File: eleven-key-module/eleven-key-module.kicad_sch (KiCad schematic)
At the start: 90 parts, among them J1 +24V, J2 FPGA PWM Outputs, Q1 2N7000, Q10 IRLB8721PBF, Q11 2N7000, Q12 IRLB8721PBF, Q13 2N7000, Q14 IRLB8721PBF, Q15 2N7000, Q16 IRLB8721PBF, Q17 2N7000, Q18 IRLB8721PBF, Q19 2N7000, Q2 IRLB8721PBF, Q20 IRLB8721PBF, Q21 2N7000, Q22 IRLB8721PBF, Q3 2N7000, Q4 IRLB8721PBF, Q5 2N7000, Q6 IRLB8721PBF, Q7 2N7000, Q8 IRLB8721PBF, Q9 2N7000

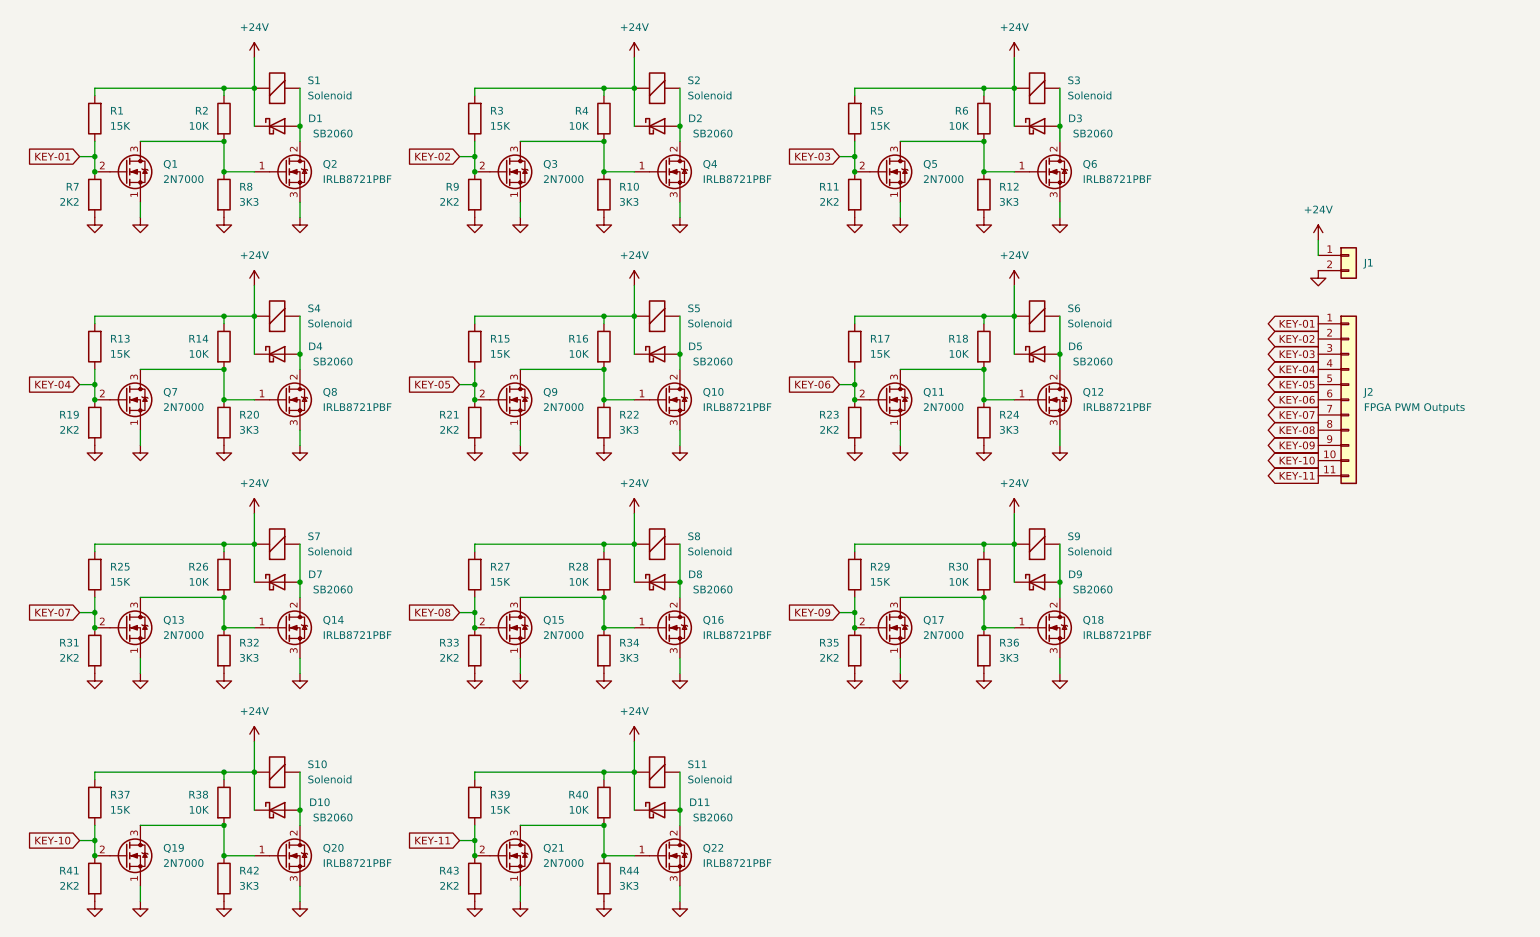
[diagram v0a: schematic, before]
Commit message: Switch schematic to Atmega328P
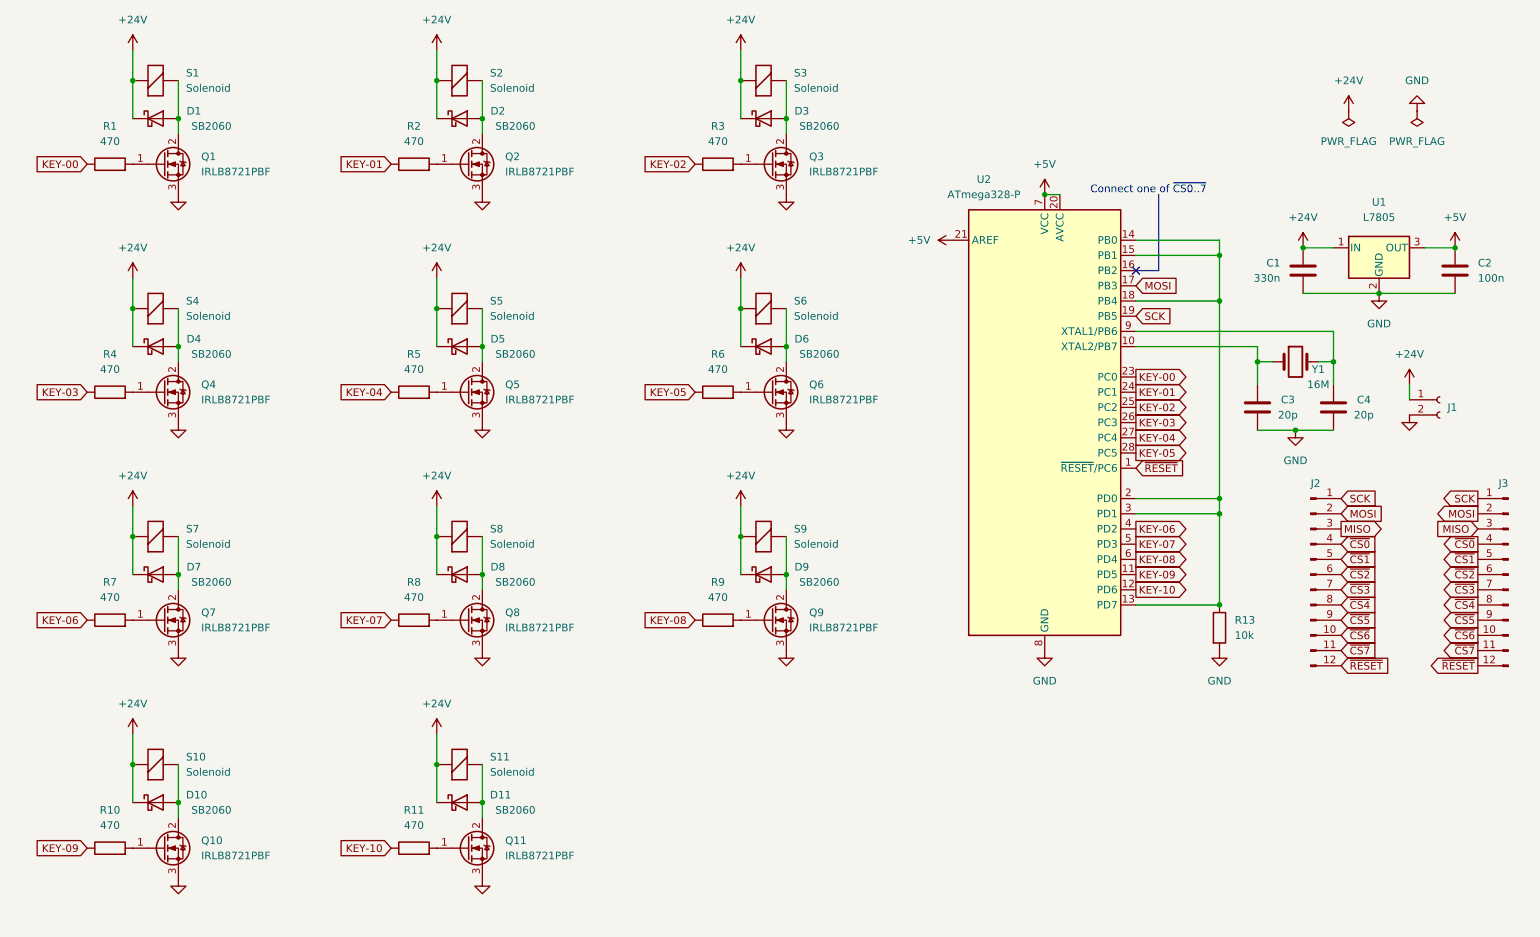
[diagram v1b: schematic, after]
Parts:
- removed J1: +24V, TerminalBlock_TE-Connectivity:TerminalBlock_TE_282834-2_1x02_P2.54mm_Horizontal, symbol Connector_Generic:Conn_01x02
- removed J2: FPGA PWM Outputs, Connector_JST:JST_XH_S11B-XH-A_1x11_P2.50mm_Horizontal, symbol Connector_Generic:Conn_01x11
- removed Q1, Q11, Q13, Q15, Q17, Q19, Q21, Q3, Q5, Q7, Q9: 2N7000, Package_TO_SOT_THT:TO-92_Inline, symbol Transistor_FET:2N7000
- removed Q12, Q14, Q16, Q18, Q20, Q22: IRLB8721PBF, Package_TO_SOT_THT:TO-220-3_Vertical, symbol Transistor_FET:IRLB8721PBF
- removed R12, R20, R22, R24, R32, R34, R36, R42, R44: 3K3, Resistor_THT:R_Axial_DIN0204_L3.6mm_D1.6mm_P2.54mm_Vertical, symbol Device:R
- removed R14, R16, R18, R26, R28, R30, R38, R40: 10K, Resistor_THT:R_Axial_DIN0204_L3.6mm_D1.6mm_P2.54mm_Vertical, symbol Device:R
- removed R15, R17, R25, R27, R29, R37, R39: 15K, Resistor_THT:R_Axial_DIN0204_L3.6mm_D1.6mm_P2.54mm_Vertical, symbol Device:R
- removed R19, R21, R23, R31, R33, R35, R41, R43: 2K2, Resistor_THT:R_Axial_DIN0204_L3.6mm_D1.6mm_P2.54mm_Vertical, symbol Device:R
- added C1: 330n, Capacitor_THT:C_Rect_L4.0mm_W2.5mm_P2.50mm, symbol Device:C
- added C2: 100n, Capacitor_THT:C_Rect_L4.0mm_W2.5mm_P2.50mm, symbol Device:C
- added C3, C4: 20p, Capacitor_THT:C_Disc_D3.4mm_W2.1mm_P2.50mm, symbol Device:C
- added J1: Conn_01x02_Female, symbol Connector:Conn_01x02_Female
- added J2, J3: Conn_01x12_Male, symbol Connector:Conn_01x12_Male
- added Q1, Q11, Q3, Q5, Q7, Q9: IRLB8721PBF, Package_TO_SOT_THT:TO-220-3_Vertical, symbol Transistor_FET:IRLB8721PBF
- added U1: L7805, Package_TO_SOT_THT:TO-220-3_Vertical, symbol Regulator_Linear:L7805
- added U2: ATmega328-P, Package_DIP:DIP-28_W7.62mm, symbol MCU_Microchip_ATmega:ATmega328-P
- added Y1: 16M, symbol Device:Crystal
- R1, R3, R5: value 15K -> 470; footprint Resistor_THT:R_Axial_DIN0204_L3.6mm_D1.6mm_P2.54mm_Vertical -> (none)
- R10, R8: value 3K3 -> 470; footprint Resistor_THT:R_Axial_DIN0204_L3.6mm_D1.6mm_P2.54mm_Vertical -> (none)
- R11, R7, R9: value 2K2 -> 470; footprint Resistor_THT:R_Axial_DIN0204_L3.6mm_D1.6mm_P2.54mm_Vertical -> (none)
- R13: value 15K -> 10k; footprint Resistor_THT:R_Axial_DIN0204_L3.6mm_D1.6mm_P2.54mm_Vertical -> (none)
- R2, R4, R6: value 10K -> 470; footprint Resistor_THT:R_Axial_DIN0204_L3.6mm_D1.6mm_P2.54mm_Vertical -> (none)
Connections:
- net +24V: now also C1.1, J1.1 (Pin_1), U1.1 (IN); no longer R1.2, R13.2, R2.1, R3.2, R4.1, R5.2, R6.1
- net GND: now also R13.2, C1.2, C2.2, C3.1, C4.1, J1.2 (Pin_2), Q1.3 (S), Q11.3 (S), Q3.3 (S), Q5.3 (S), Q7.3 (S), Q9.3 (S), U1.2 (GND), U2.22 (GND), U2.8 (GND); no longer R10.2, R11.2, R7.2, R8.2, R9.2
- net KEY-01: now also R2.1, U2.24 (PC1); no longer R1.1, R7.1
- net KEY-02: now also U2.25 (PC2); no longer R9.1
- net KEY-03: now also R4.1, U2.26 (PC3); no longer R11.1, R5.1
- net KEY-04: now also R5.1, U2.27 (PC4); no longer R13.1
- net KEY-05: now also R6.1, U2.28 (PC5)
- net KEY-06: now also R7.1, U2.4 (PD2)
- net KEY-07: now also R8.1, U2.5 (PD3)
- net KEY-08: now also R9.1, U2.6 (PD4)
- net KEY-09: now also R10.1, U2.11 (PD5)
- net KEY-10: now also R11.1, U2.12 (PD6)
- net at Q2.1 (G), R2.2: no longer R8.1
- net at D2.2 (A), S2.2 (+): now also Q2.2 (D); no longer Q4.2 (D)
- net at D1.2 (A), S1.2 (+): now also Q1.2 (D); no longer Q2.2 (D)
- net at Q4.1 (G), R4.2: no longer R10.1
- net at D8.2 (A), S8.2 (+): now also Q8.2 (D)
- net at D9.2 (A), S9.2 (+): now also Q9.2 (D)
- net at D10.2 (A), S10.2 (+): now also Q10.2 (D)
- net at D7.2 (A), S7.2 (+): now also Q7.2 (D)
- net at Q10.1 (G): now also R10.2
- net at D5.2 (A), S5.2 (+): now also Q5.2 (D); no longer Q10.2 (D)
- net at D6.2 (A), S6.2 (+): now also Q6.2 (D)
- net at D3.2 (A), S3.2 (+): now also Q3.2 (D); no longer Q6.2 (D)
- net at D11.2 (A), S11.2 (+): now also Q11.2 (D)
- net at D4.2 (A), S4.2 (+): now also Q4.2 (D); no longer Q8.2 (D)
- net at Q8.1 (G): now also R8.2
- new net: Q5.1 (G), R5.2
- new net: Q9.1 (G), R9.2
- new net: C3.2, U2.10 (XTAL2/PB7), Y1.1
- new net: R13.1, U2.13 (PD7), U2.14 (PB0), U2.15 (PB1), U2.18 (PB4), U2.2 (PD0), U2.3 (PD1)
- new net: C4.2, U2.9 (XTAL1/PB6), Y1.2
- new net: Q11.1 (G), R11.2
- new net: Q7.1 (G), R7.2
- new net: Q1.1 (G), R1.2
- new net: Q3.1 (G), R3.2
- new net +5V: C2.1, U1.3 (OUT), U2.20 (AVCC), U2.21 (AREF), U2.7 (VCC)
- new net KEY-00: R1.1, U2.23 (PC0)
- new net MISO: J2.3 (Pin_3), J3.3 (Pin_3)
- new net MOSI: J2.2 (Pin_2), J3.2 (Pin_2), U2.17 (PB3)
- new net SCK: J2.1 (Pin_1), J3.1 (Pin_1), U2.19 (PB5)
- new net ~{CS0}: J2.4 (Pin_4), J3.4 (Pin_4)
- new net ~{CS1}: J2.5 (Pin_5), J3.5 (Pin_5)
- new net ~{CS2}: J2.6 (Pin_6), J3.6 (Pin_6)
- new net ~{CS3}: J2.7 (Pin_7), J3.7 (Pin_7)
- new net ~{CS4}: J2.8 (Pin_8), J3.8 (Pin_8)
- new net ~{CS5}: J2.9 (Pin_9), J3.9 (Pin_9)
- new net ~{CS6}: J2.10 (Pin_10), J3.10 (Pin_10)
- new net ~{CS7}: J2.11 (Pin_11), J3.11 (Pin_11)
- new net ~{RESET}: J2.12 (Pin_12), J3.12 (Pin_12), U2.1 (~{RESET}/PC6)
- no-connect marks 0 -> 1
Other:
- note added: "Connect one of ~{CS0..7}"
- title: (none) -> Eleven-Key Module
- moved on the sheet: D1, S1

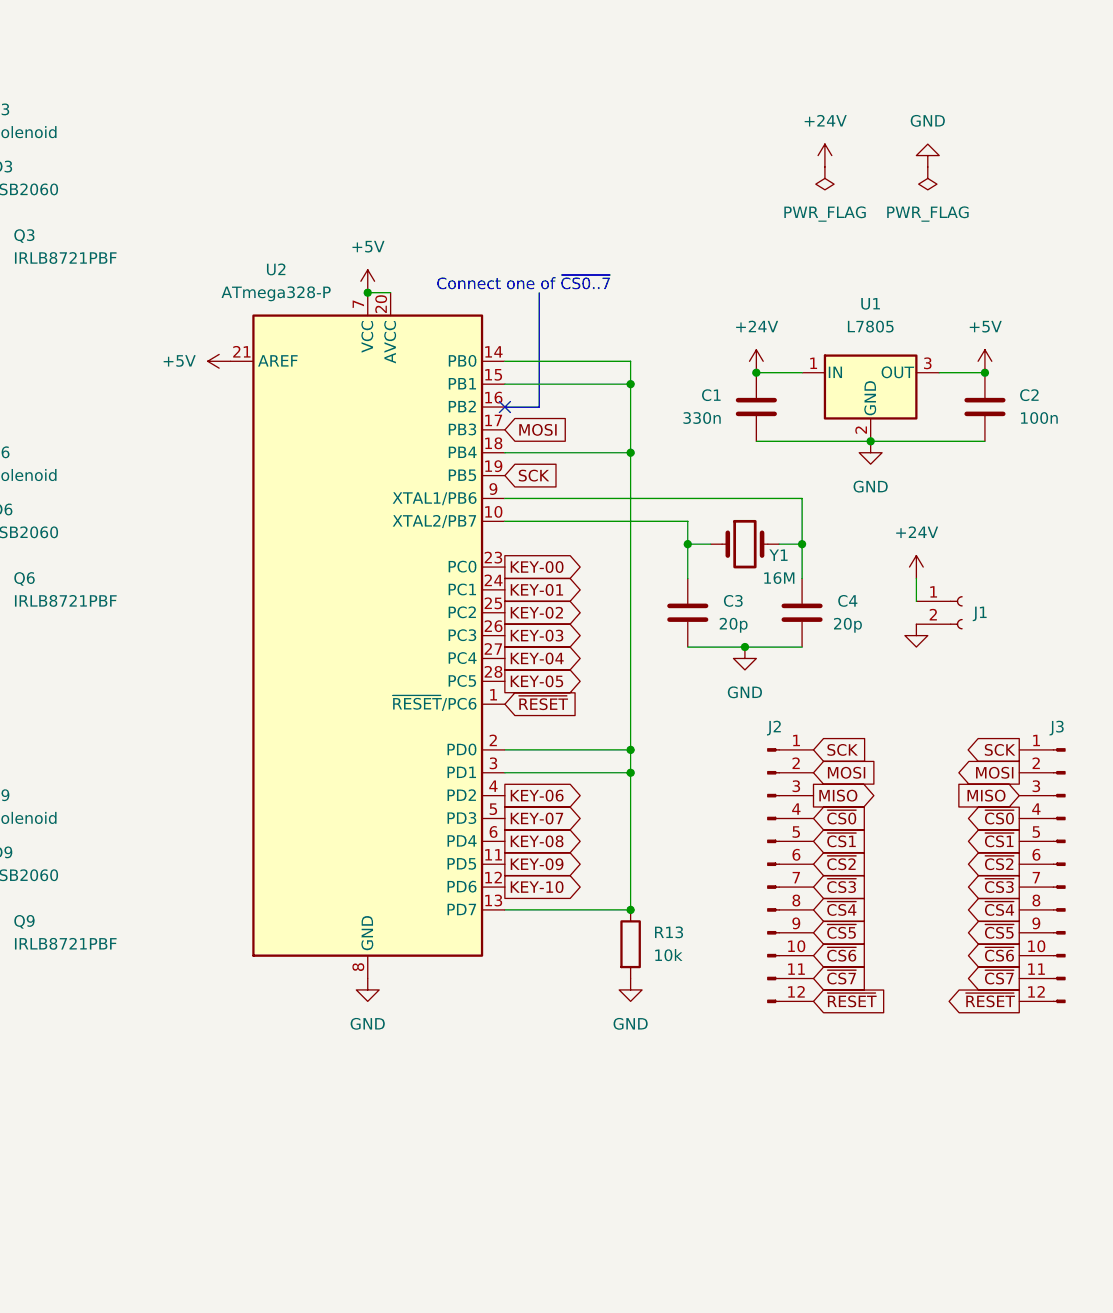
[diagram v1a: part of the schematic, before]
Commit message: Update KiCad version and convert schematic to I2C
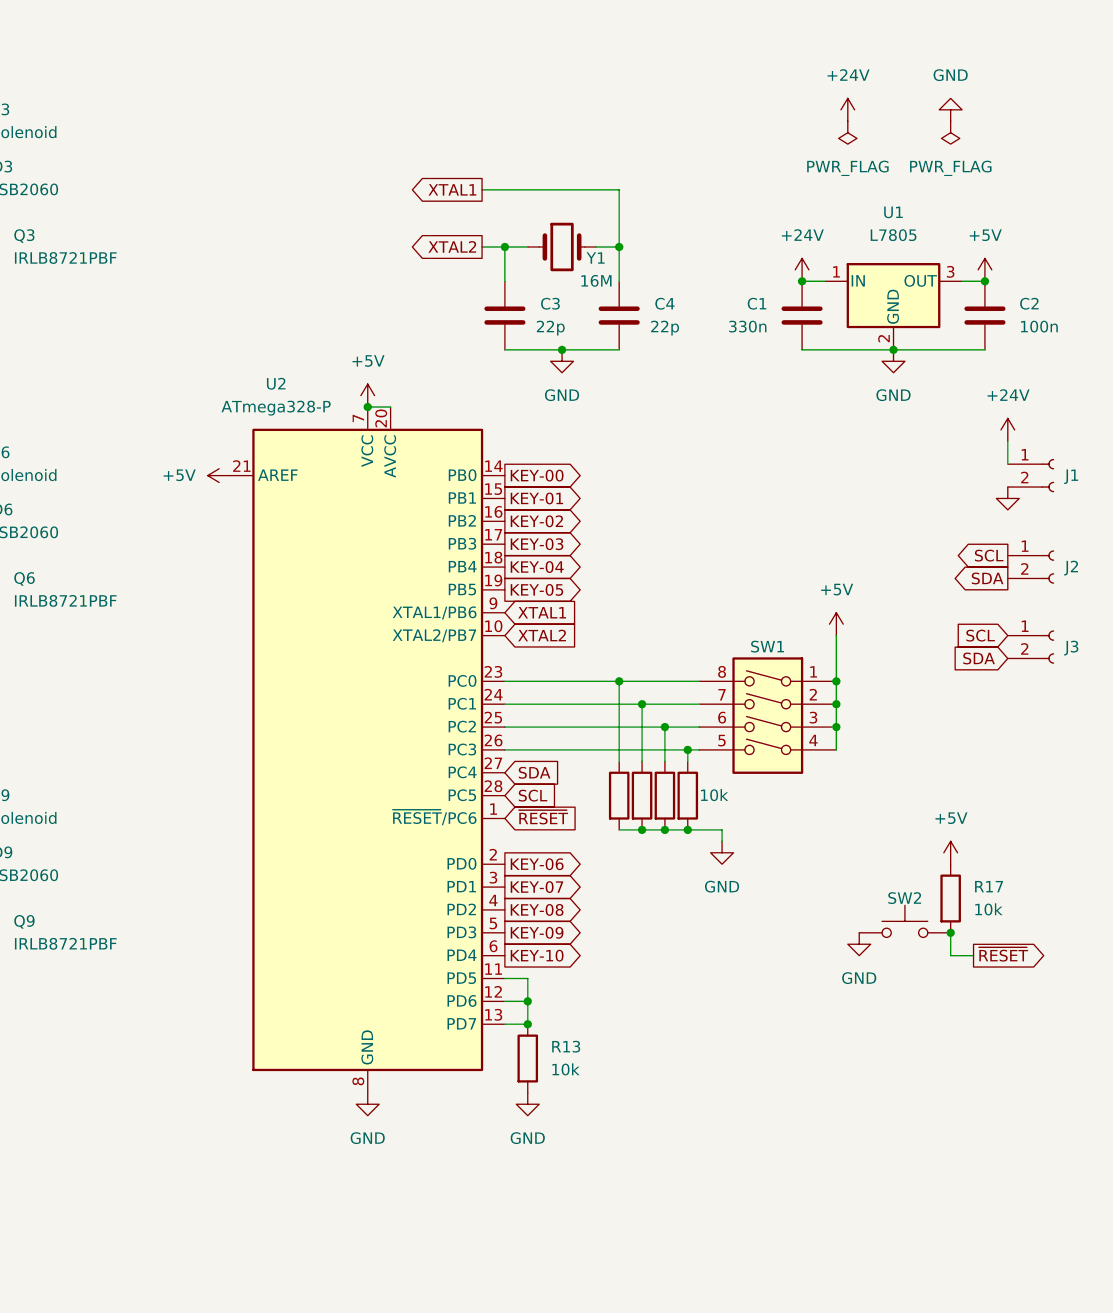
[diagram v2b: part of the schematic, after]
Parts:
- removed J2, J3: Conn_01x12_Male, symbol Connector:Conn_01x12_Male
- added J2, J3: Conn_01x02_Female, symbol Connector:Conn_01x02_Female
- added R12, R14, R15, R16, R17: 10k, symbol Device:R
- added SW1: SW_DIP_x04, symbol Switch:SW_DIP_x04
- added SW2: SW_Push, symbol Switch:SW_Push
- C3, C4: value 20p -> 22p
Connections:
- net MOSI is gone; now on net KEY-03: U2.17 (PB3)
- net SCK is gone; now on net KEY-05: U2.19 (PB5)
- net +5V: now also R17.1, SW1.1, SW1.2, SW1.3, SW1.4
- net GND: now also R12.2, R14.2, R15.2, R16.2, SW2.1
- net KEY-00: now also U2.14 (PB0); no longer U2.23 (PC0)
- net KEY-01: now also U2.15 (PB1); no longer U2.24 (PC1)
- net KEY-02: now also U2.16 (PB2); no longer U2.25 (PC2)
- net KEY-03: no longer U2.26 (PC3)
- net KEY-04: now also U2.18 (PB4); no longer U2.27 (PC4)
- net KEY-05: no longer U2.28 (PC5)
- net KEY-06: now also U2.2 (PD0); no longer U2.4 (PD2)
- net KEY-07: now also U2.3 (PD1); no longer U2.5 (PD3)
- net KEY-08: now also U2.4 (PD2); no longer U2.6 (PD4)
- net KEY-09: now also U2.5 (PD3); no longer U2.11 (PD5)
- net KEY-10: now also U2.6 (PD4); no longer U2.12 (PD6)
- net ~{RESET}: now also R17.2, SW2.2
- net XTAL2: now reaches C3.2, U2.10 (XTAL2/PB7), Y1.1
- net XTAL1: now reaches C4.2, U2.9 (XTAL1/PB6), Y1.2
- new net: R14.1, SW1.6, U2.25 (PC2)
- new net: R13.1, U2.11 (PD5), U2.12 (PD6), U2.13 (PD7)
- new net: R16.1, SW1.8, U2.23 (PC0)
- new net: R15.1, SW1.7, U2.24 (PC1)
- new net: R12.1, SW1.5, U2.26 (PC3)
- new net SCL: J2.1 (Pin_1), J3.1 (Pin_1), U2.28 (PC5)
- new net SDA: J2.2 (Pin_2), J3.2 (Pin_2), U2.27 (PC4)
- no-connect marks 1 -> 0
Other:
- note removed: "Connect one of ~{CS0..7}"
- moved on the sheet: C1, C2, C3, C4, J1, R13, U1, U2, Y1

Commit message: Further update schematic and create PCB
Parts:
- removed C2: 100n, Capacitor_THT:C_Rect_L4.0mm_W2.5mm_P2.50mm, symbol Device:C
- removed R13: 10k, symbol Device:R
- removed S1, S10, S11, S2, S3, S4, S5, S6, S7, S8, S9: Solenoid, TerminalBlock_TE-Connectivity:TerminalBlock_TE_282834-2_1x02_P2.54mm_Horizontal, symbol Device:ElectromagneticActor
- removed U1: L7805, Package_TO_SOT_THT:TO-220-3_Vertical, symbol Regulator_Linear:L7805
- added D12: LED, LED_THT:LED_D5.0mm, symbol Device:LED
- added J4: Conn_01x12_Socket, TerminalBlock:TerminalBlock_Xinya_XY308-2.54-12P_1x12_P2.54mm_Horizontal, symbol Connector:Conn_01x12_Socket
- added J5: Conn_01x10_Socket, TerminalBlock:TerminalBlock_Xinya_XY308-2.54-10P_1x10_P2.54mm_Horizontal, symbol Connector:Conn_01x10_Socket
- added R17: 470, Resistor_THT:R_Axial_DIN0204_L3.6mm_D1.6mm_P7.62mm_Horizontal, symbol Device:R
- C1: value 330n -> 100n; footprint Capacitor_THT:C_Rect_L4.0mm_W2.5mm_P2.50mm -> Capacitor_THT:C_Rect_L4.6mm_W3.8mm_P2.50mm_MKS02_FKP02
- C2: renamed from C3; footprint Capacitor_THT:C_Disc_D3.4mm_W2.1mm_P2.50mm -> Capacitor_THT:C_Rect_L4.0mm_W2.5mm_P2.50mm
- C3: renamed from C4; footprint Capacitor_THT:C_Disc_D3.4mm_W2.1mm_P2.50mm -> Capacitor_THT:C_Rect_L4.0mm_W2.5mm_P2.50mm
- J1: value Conn_01x02_Female -> Conn_01x03_Socket; footprint (none) -> TerminalBlock:TerminalBlock_Xinya_XY308-2.54-3P_1x03_P2.54mm_Horizontal; symbol Connector:Conn_01x02_Female -> Connector:Conn_01x03_Socket
- J2, J3: footprint (none) -> Connector_PinHeader_2.54mm:PinHeader_1x02_P2.54mm_Vertical
- R1, R10, R11, R14, R2, R3, R4, R5, R6, R7, R8, R9: footprint (none) -> Resistor_THT:R_Axial_DIN0204_L3.6mm_D1.6mm_P7.62mm_Horizontal
- R12: renamed from R16; footprint (none) -> Resistor_THT:R_Axial_DIN0204_L3.6mm_D1.6mm_P7.62mm_Horizontal
- R13: renamed from R15; footprint (none) -> Resistor_THT:R_Axial_DIN0204_L3.6mm_D1.6mm_P7.62mm_Horizontal
- R15: renamed from R12; footprint (none) -> Resistor_THT:R_Axial_DIN0204_L3.6mm_D1.6mm_P7.62mm_Horizontal
- R16: renamed from R17; footprint (none) -> Resistor_THT:R_Axial_DIN0204_L3.6mm_D1.6mm_P7.62mm_Horizontal
- SW1: footprint (none) -> Package_DIP:DIP-8_W7.62mm
- SW2: footprint (none) -> Button_Switch_THT:SW_PUSH_6mm
- Y1: footprint (none) -> Crystal:Crystal_HC49-U_Vertical
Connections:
- net +24V: now also J4.1 (Pin_1), J4.11 (Pin_11), J4.3 (Pin_3), J4.5 (Pin_5), J4.7 (Pin_7), J4.9 (Pin_9), J5.1 (Pin_1), J5.3 (Pin_3), J5.5 (Pin_5), J5.7 (Pin_7), J5.9 (Pin_9); no longer C1.1
- net +5V: now also C1.1, J1.2 (Pin_2); no longer U2.21 (AREF)
- net GND: now also J1.3 (Pin_3), R17.2; no longer J1.2 (Pin_2)
- net S04: now reaches D4.2 (A), Q4.2 (D)
- net S04: now also J4.8 (Pin_8)
- net S05: now reaches D5.2 (A), Q5.2 (D)
- net S05: now also J4.10 (Pin_10)
- net S09: now reaches D9.2 (A), Q9.2 (D)
- net S09: now also J5.6 (Pin_6)
- net S11: now reaches D11.2 (A), Q11.2 (D)
- net S11: now also J5.10 (Pin_10)
- net S08: now reaches D8.2 (A), Q8.2 (D)
- net S08: now also J5.4 (Pin_4)
- net S01: now reaches D1.2 (A), Q1.2 (D)
- net S01: now also J4.2 (Pin_2)
- net S02: now reaches D2.2 (A), Q2.2 (D)
- net S02: now also J4.4 (Pin_4)
- net at U2.12 (PD6), U2.13 (PD7): now also D12.1 (K), R17.1; no longer U2.11 (PD5)
- net S06: now reaches D6.2 (A), Q6.2 (D)
- net S06: now also J4.12 (Pin_12)
- net S10: now reaches D10.2 (A), Q10.2 (D)
- net S10: now also J5.8 (Pin_8)
- net S07: now reaches D7.2 (A), Q7.2 (D)
- net S07: now also J5.2 (Pin_2)
- net S03: now reaches D3.2 (A), Q3.2 (D)
- net S03: now also J4.6 (Pin_6)
- net KEY-00 renamed K01
- net KEY-01 renamed K02
- net KEY-02 renamed K03
- net KEY-03 renamed K04
- net KEY-04 renamed K05
- net KEY-05 renamed K06
- net KEY-06 renamed K07
- net KEY-07 renamed K08
- net KEY-08 renamed K09
- net KEY-09 renamed K10
- net KEY-10 renamed K11
- new net: D12.2 (A), U2.11 (PD5)
- no-connect marks 0 -> 1
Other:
- moved on the sheet: C2, C3, Y1
